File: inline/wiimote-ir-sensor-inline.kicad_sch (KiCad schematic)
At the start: 10 parts, among them J1 Conn_01x04_Pin, U2 AP2112-3.3V, X1 SG3225CAN 24.0000M-TJGA3

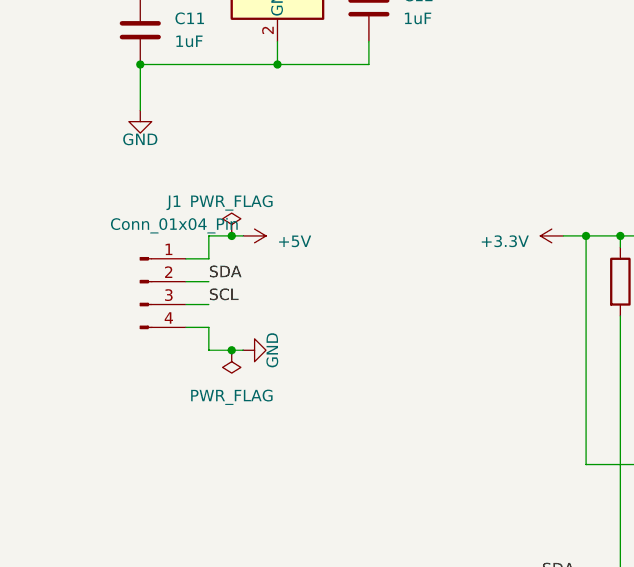
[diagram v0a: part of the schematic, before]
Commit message: Revision 2.
- Reroute to leave more empty space on sides
- Tweak camera footprint
- Add castellated variant
- Add manually panelised boards to help prevent panel tabs
  from appearing in edge connector
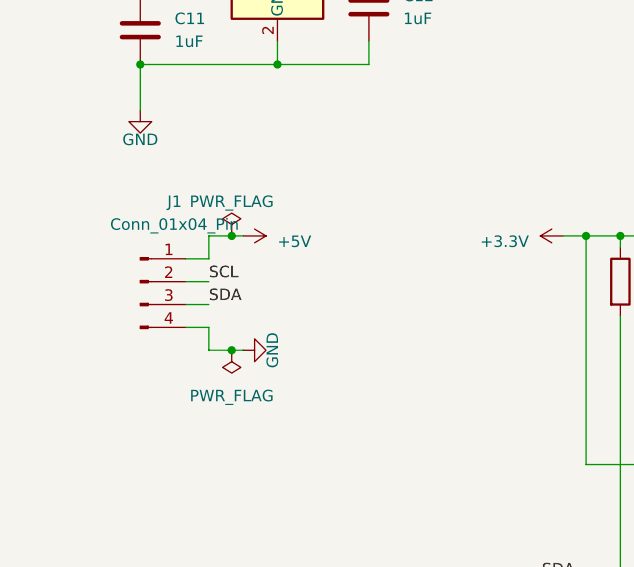
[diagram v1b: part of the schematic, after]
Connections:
- net SCL: now also J1.2 (Pin_2); no longer J1.3 (Pin_3)
- net SDA: now also J1.3 (Pin_3); no longer J1.2 (Pin_2)
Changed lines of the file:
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@@
     (effects (font (size 1.27 1.27)) (justify right bottom))
   )
-  (label "SDA" (at 72.39 81.28 0) (fields_autoplaced)
+  (label "SDA" (at 72.39 83.82 0) (fields_autoplaced)
     (effects (font (size 1.27 1.27)) (justify left bottom))
   )
-  (label "SCL" (at 72.39 83.82 0) (fields_autoplaced)
+  (label "SCL" (at 72.39 81.28 0) (fields_autoplaced)
     (effects (font (size 1.27 1.27)) (justify left bottom))
   )

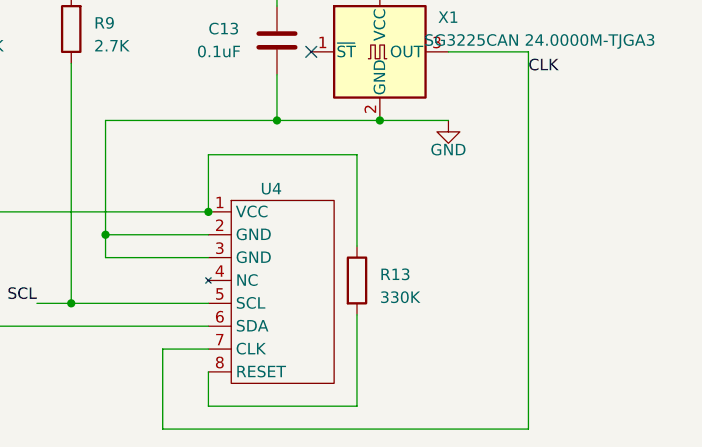
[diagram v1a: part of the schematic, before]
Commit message: Fix BOM and schematic R3 value
(Thanks to RetroMidget for spotting this!)
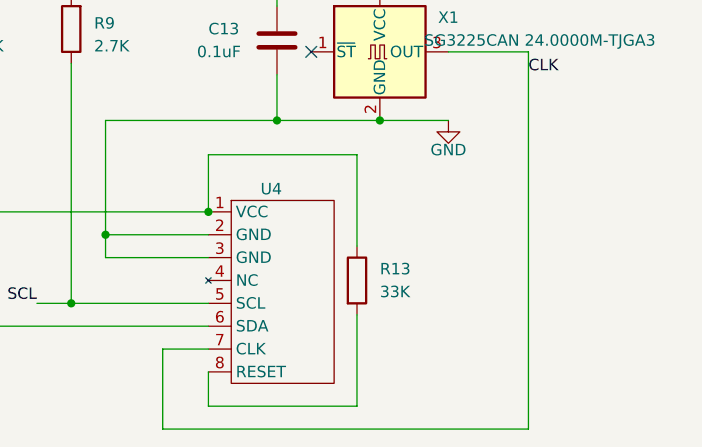
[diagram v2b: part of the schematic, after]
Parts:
- R13: value 330K -> 33K

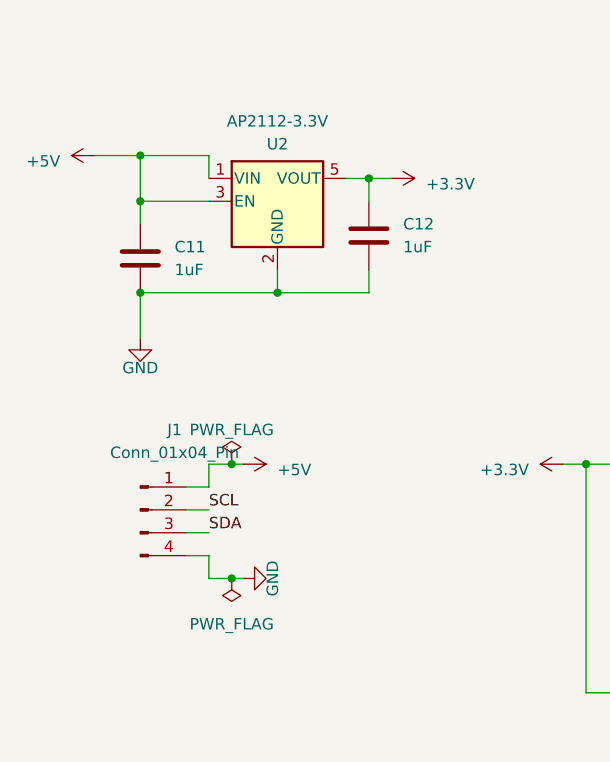
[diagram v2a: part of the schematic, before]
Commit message: Instate superslim variant as new inline
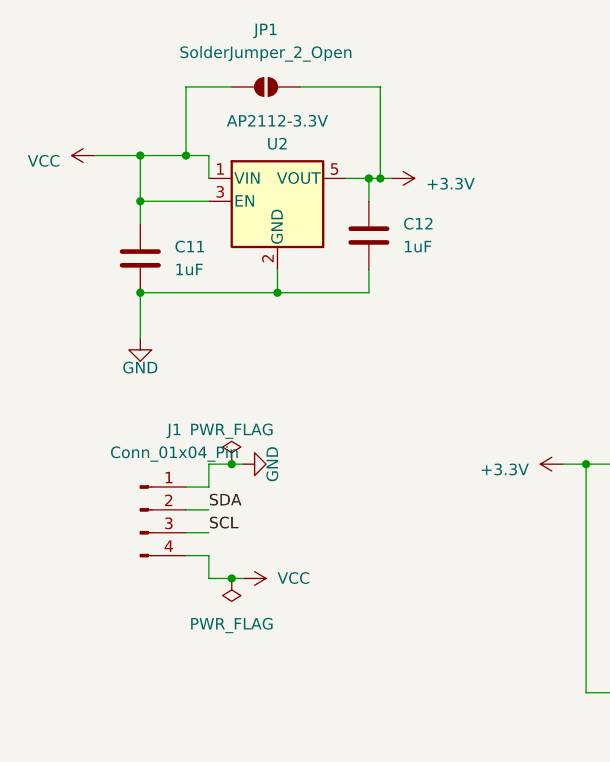
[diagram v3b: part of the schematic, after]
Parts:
- added JP1: SolderJumper_2_Open, Jumper:SolderJumper-2_P1.3mm_Open_RoundedPad1.0x1.5mm, symbol Jumper:SolderJumper_2_Open
- C11, C12: LCSC (none) -> C519560
- C13: LCSC (none) -> C14663
- J1: footprint Connector_PinHeader_2.54mm:PinHeader_1x04_P2.54mm_Vertical -> Connector_PinHeader_2.00mm:PinHeader_1x04_P2.00mm_Vertical
- R13: LCSC (none) -> C126359
- R8, R9: LCSC (none) -> C114612
- U2: LCSC (none) -> C51118
- U4: footprint GUN4IR:wiimote-pixart-camera-inline -> GUN4IR:wiimote-pixart-camera-inline_slim
- X1: LCSC (none) -> C5203548
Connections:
- net +3.3V: now also JP1.2 (B)
- net GND: now also J1.1 (Pin_1); no longer J1.4 (Pin_4)
- net SCL: now also J1.3 (Pin_3); no longer J1.2 (Pin_2)
- net SDA: now also J1.2 (Pin_2); no longer J1.3 (Pin_3)
- net +5V renamed VCC
- net VCC: now also J1.4 (Pin_4), JP1.1 (A); no longer J1.1 (Pin_1)

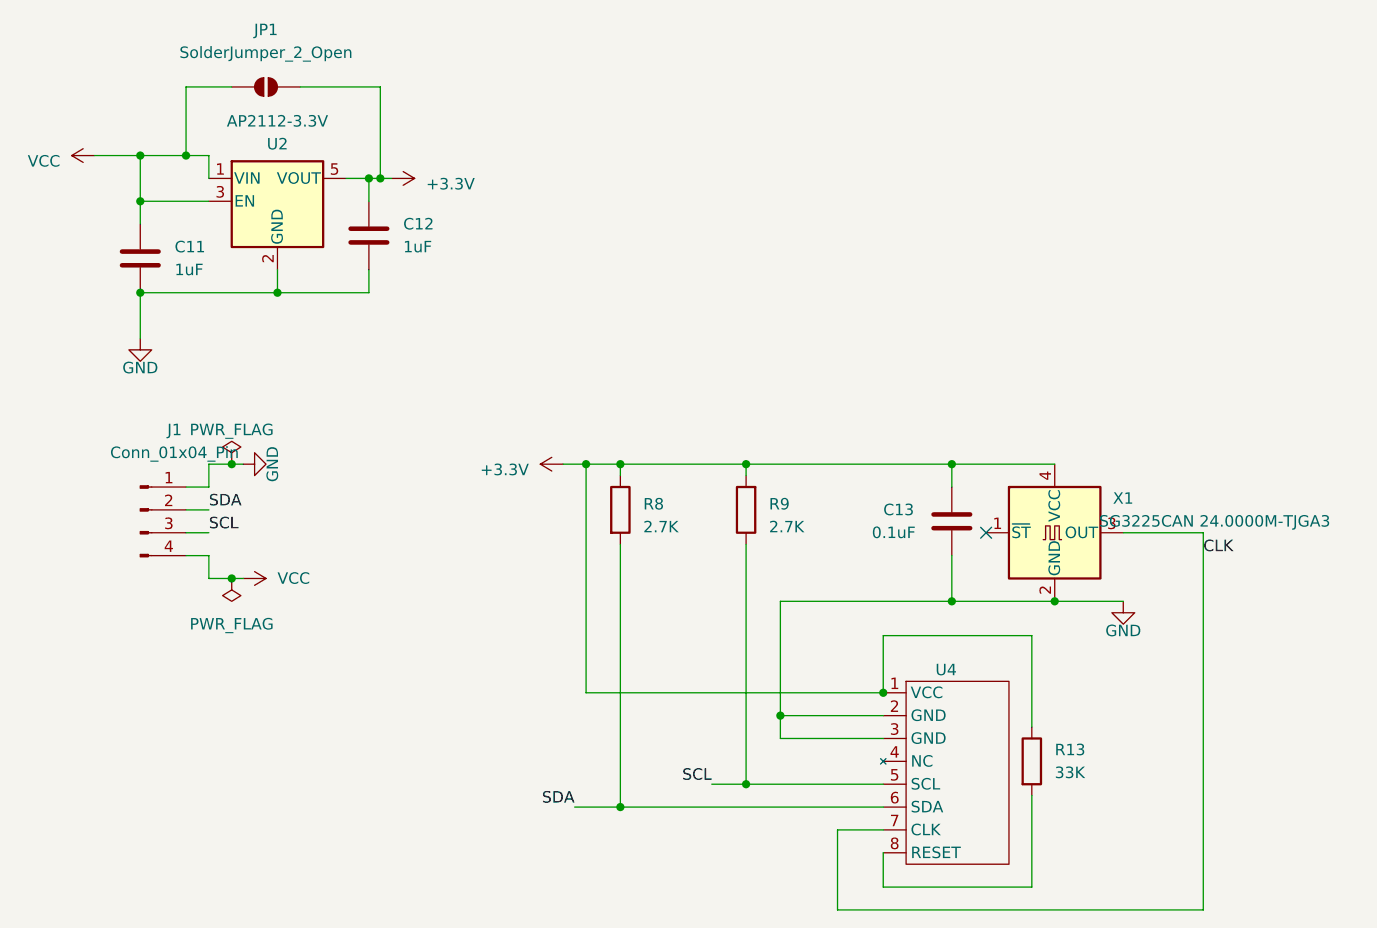
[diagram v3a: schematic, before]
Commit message: Update inline board to allow wiring clock signal directly
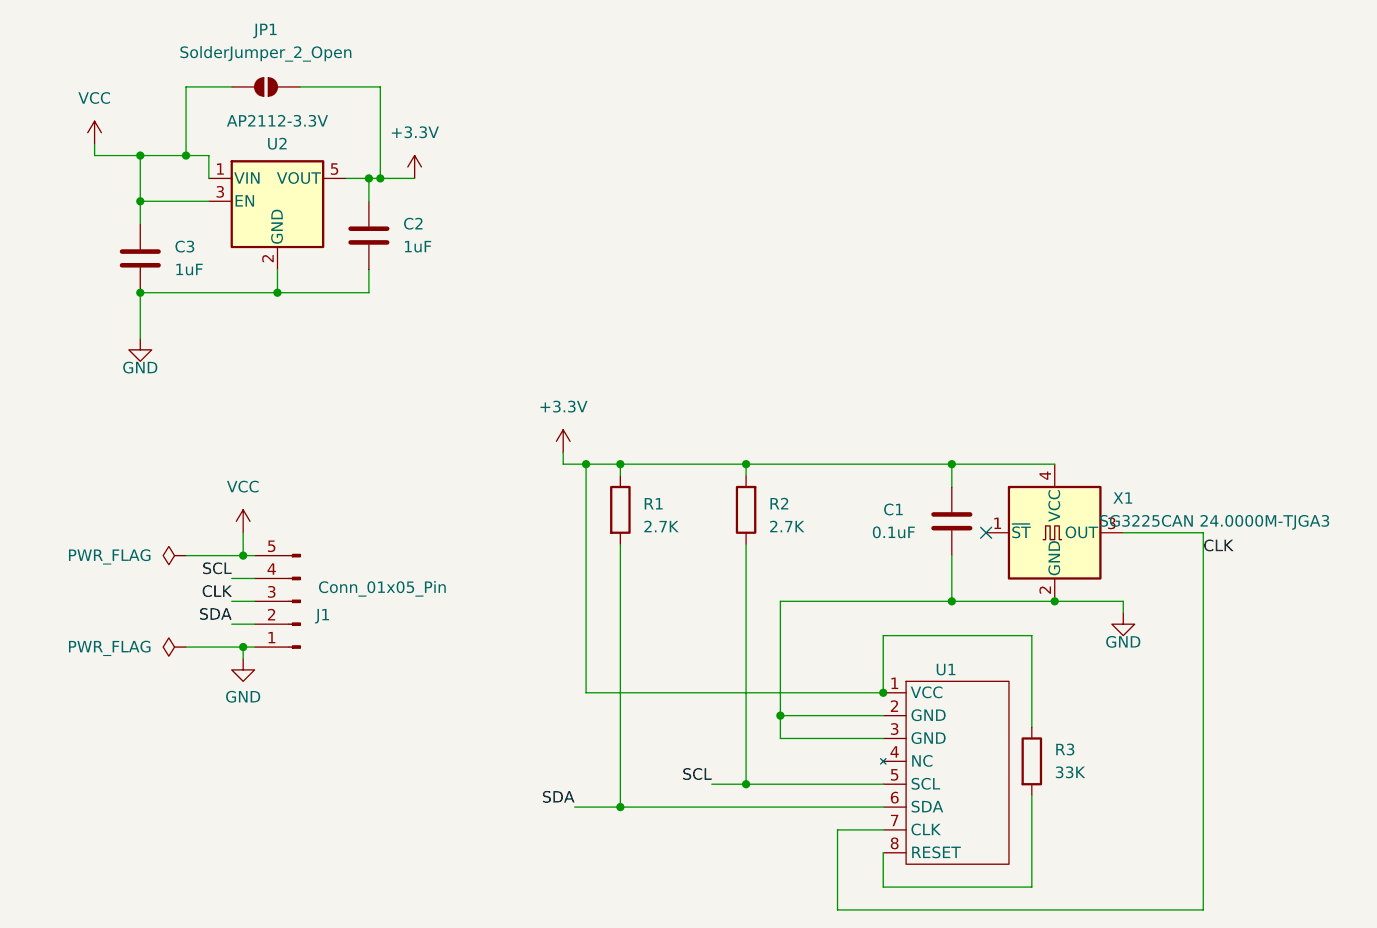
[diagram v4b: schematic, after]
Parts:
- J1: value Conn_01x04_Pin -> Conn_01x05_Pin; footprint Connector_PinHeader_2.00mm:PinHeader_1x04_P2.00mm_Vertical -> wiimote-ir-sensor:5Wires-staggered; symbol Connector:Conn_01x04_Pin -> Connector:Conn_01x05_Pin
- U1: renamed from U4; footprint GUN4IR:wiimote-pixart-camera-inline_slim -> wiimote-ir-sensor:wiimote-pixart-camera-inline_slim
- renumbered C13 to C1, C12 to C2, C11 to C3, R8 to R1, R9 to R2, R13 to R3
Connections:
- net CLK: now also J1.3 (Pin_3)
- net SCL: now also J1.4 (Pin_4); no longer J1.3 (Pin_3)
- net VCC: now also J1.5 (Pin_5); no longer J1.4 (Pin_4)
